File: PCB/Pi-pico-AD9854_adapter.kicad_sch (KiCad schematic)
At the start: 15 parts, among them J1 Conn_02x20_Odd_Even, J2 TYPE-C-31-M-12, J3 Conn_01x01_Male, J4 Screw_Terminal_01x02, U1 Pico, U2 LM3940IMP-3.3, U3 DMG2305UX-13

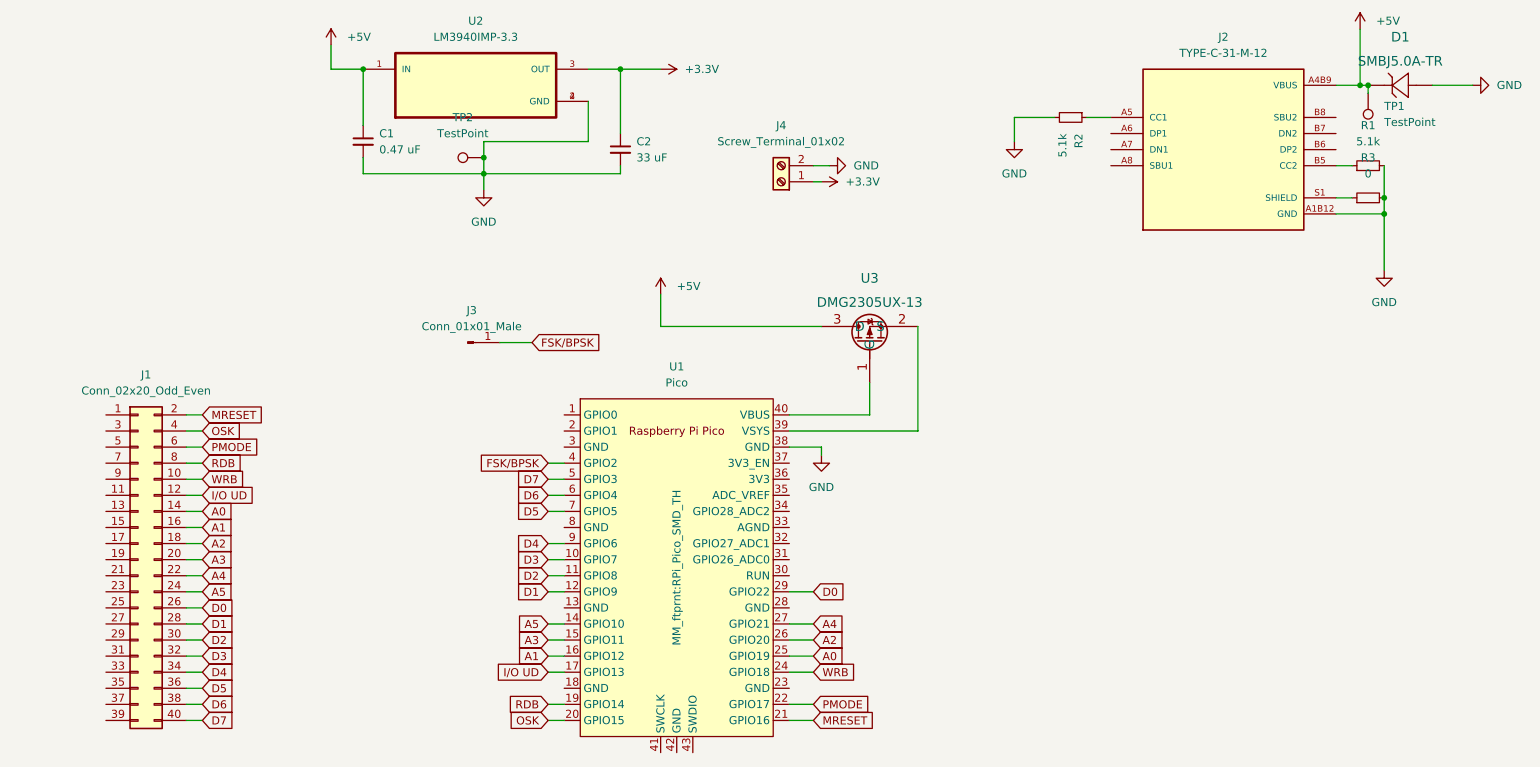
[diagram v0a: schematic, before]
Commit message: V1.0_beta prototype. Firwmare fixes
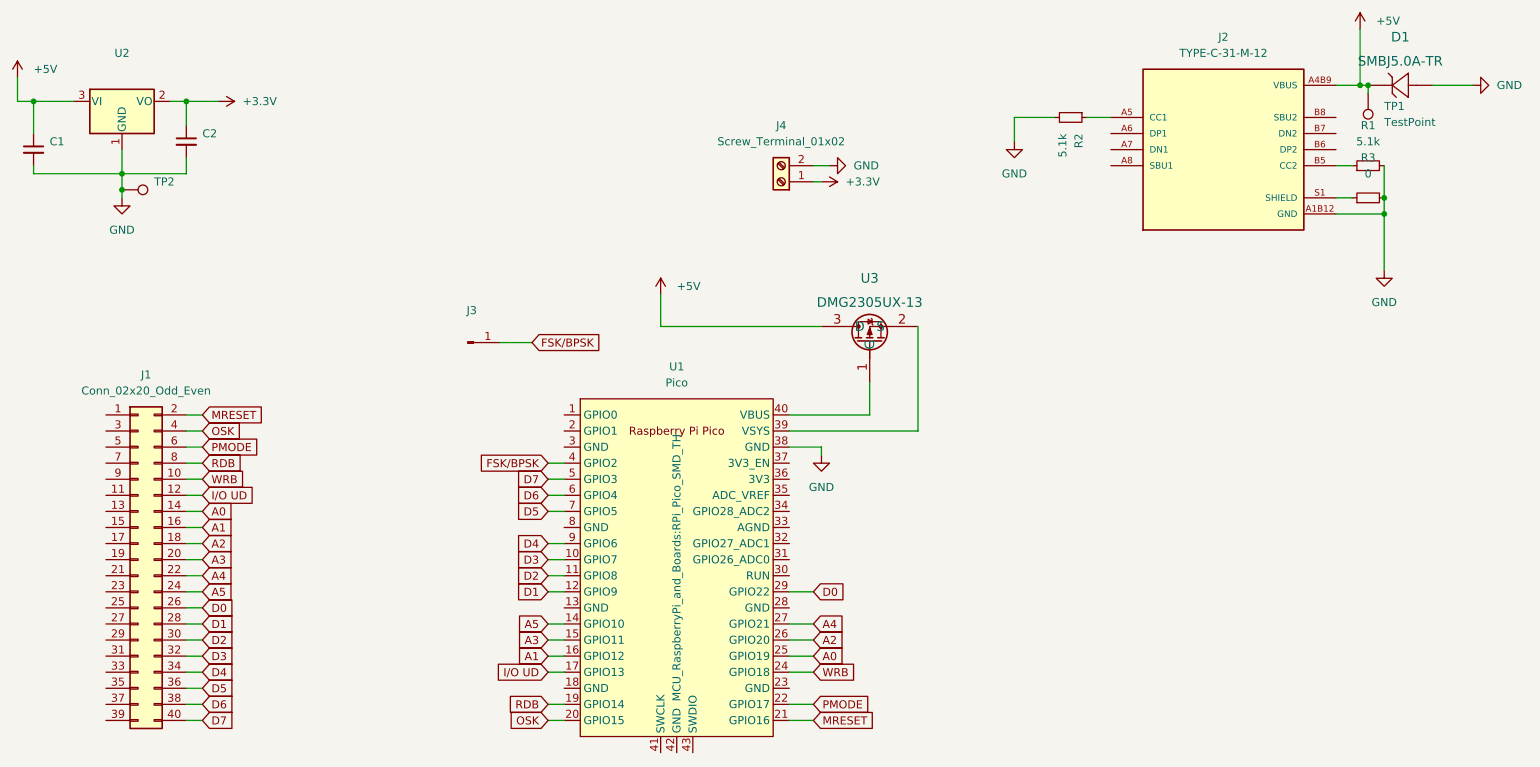
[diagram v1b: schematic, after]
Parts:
- removed U2: LM3940IMP-3.3, MM_ftprnt:SOT230P700X180-4N, symbol LM3940IMP-3.3:LM3940IMP-3.3
- added U2: (no value), symbol Regulator_Linear:LT1086-3.3
- C1: value 0.47 uF -> (none); footprint Capacitor_SMD:C_0805_2012Metric -> (none)
- C2: value 33 uF -> (none); footprint Capacitor_SMD:C_0805_2012Metric -> (none)
- D1: footprint MM_ftprnt:SMBJ5.0A-TR -> SMBJ5-0A-TR:SMBJ5.0A-TR
- J2: footprint MM_ftprnt:HRO_TYPE-C-31-M-12 -> HRO_TYPE-C-31-M-12
- J3: value Conn_01x01_Male -> (none); footprint Connector_PinHeader_1.27mm:PinHeader_1x01_P1.27mm_Vertical -> (none)
- TP2: value TestPoint -> (none); footprint TestPoint:TestPoint_THTPad_D2.0mm_Drill1.0mm -> (none)
- U1: footprint MM_ftprnt:RPi_Pico_SMD_TH -> MCU_RaspberryPi_and_Boards:RPi_Pico_SMD_TH
- U3: footprint MM_ftprnt:DMG2305UX-13 -> footprints:DMG2305UX-13
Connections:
- net +3V3: now also U2.2 (VO)
- net +5V: now also U2.3 (VI)
- net GND: now also U2.1 (GND)
